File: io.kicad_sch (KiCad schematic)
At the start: 20 parts, among them J3 USB_C_Receptacle_USB2.0, J4 Conn_01x06_Male, U3 USBLC6-2SC6

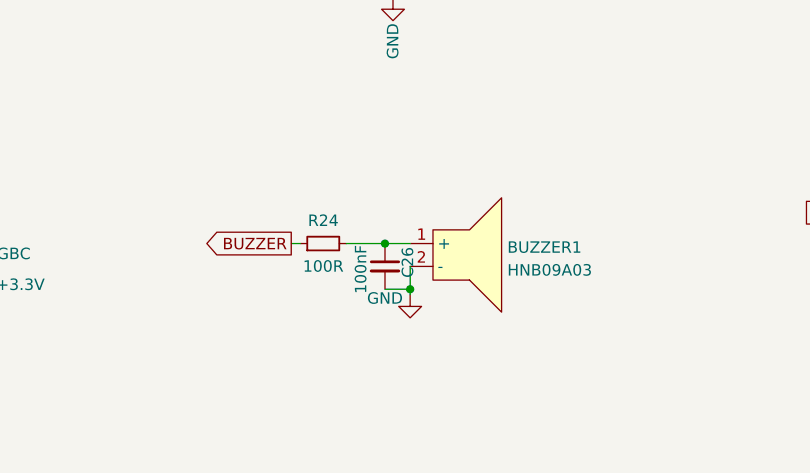
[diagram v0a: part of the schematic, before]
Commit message: cut outs design in place
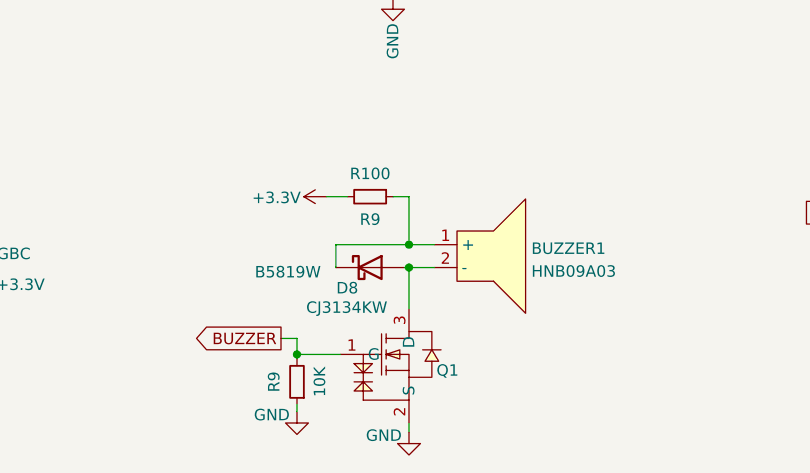
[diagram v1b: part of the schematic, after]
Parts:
- removed C26: 100nF, Capacitor_SMD:C_0402_1005Metric, symbol Device:C_Small
- removed R24: 100R, Resistor_SMD:R_0402_1005Metric, symbol Device:R_Small
- added D8: B5819W, Diode_SMD:D_SOD-123, symbol Diode:MBR0530
- added Q1: CJ3134KW, easyeda2kicad:SC-70-3_L2.1-W1.3-P1.30-LS2.1-BR, symbol easyeda:CJ3134KW
- added R9: 10K, Resistor_SMD:R_0402_1005Metric, symbol Device:R_Small
- added R9: R100, Resistor_SMD:R_0402_1005Metric, symbol Device:R_Small
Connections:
- net +3.3V: now also R9.2
- net BUZZER: now also Q1.1 (G), R9.2
- net GND: now also Q1.2 (S), R9.1; no longer BUZZER1.2 (-)
- net at BUZZER1.1 (+): now also D8.1 (K), R9.1
- new net: BUZZER1.2 (-), D8.2 (A), Q1.3 (D)
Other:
- moved on the sheet: BUZZER1

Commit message: kicad 8
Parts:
- renumbered Q1 to Q5, R9 to R24, R9 to R26
